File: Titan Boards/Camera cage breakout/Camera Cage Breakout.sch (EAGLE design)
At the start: 10 parts, among them IC1 LM741D, T2 2N2222

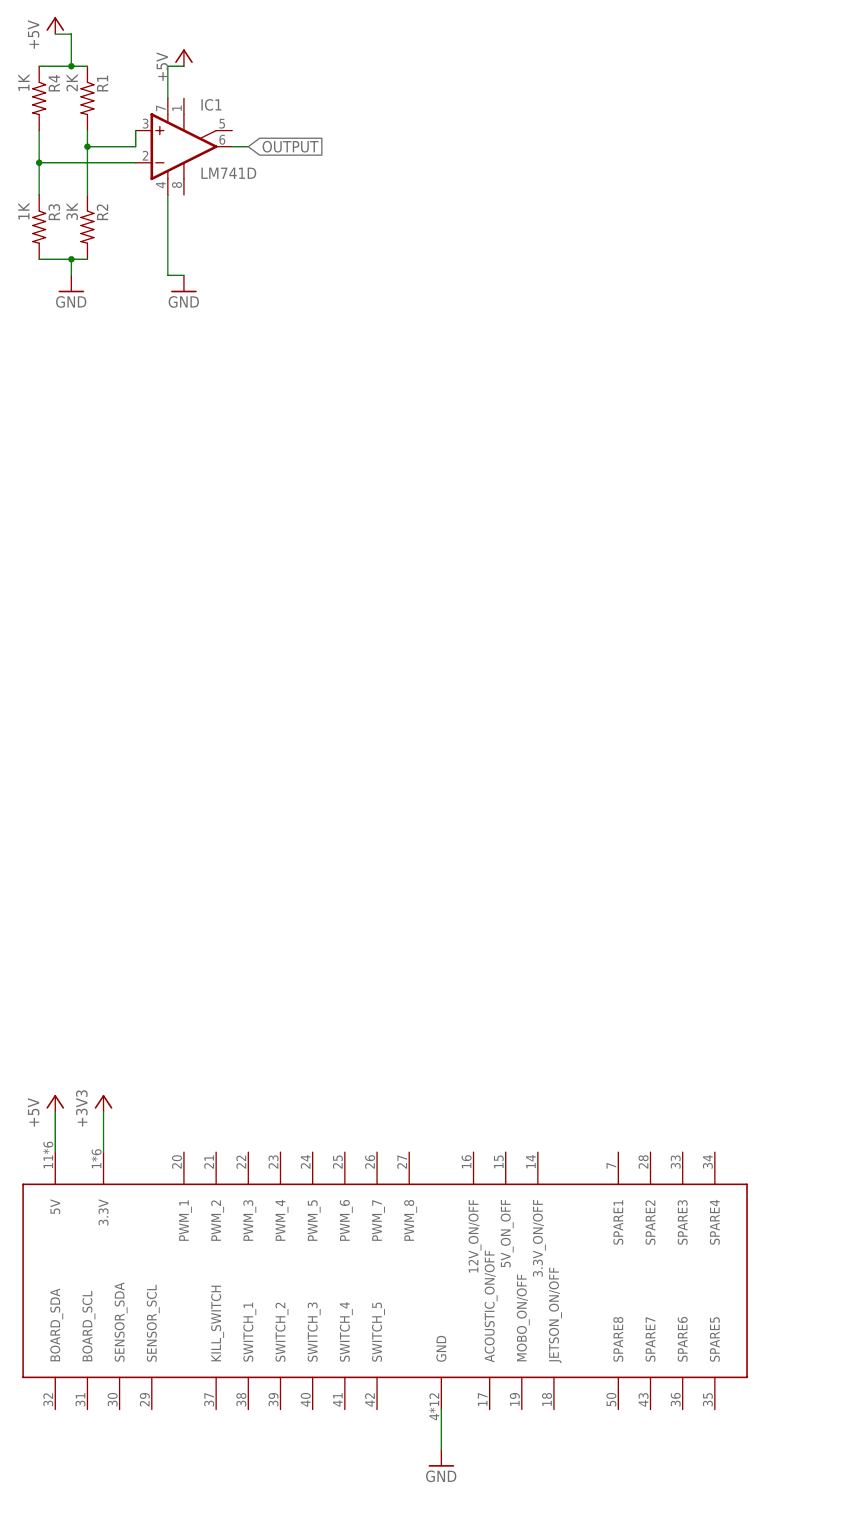
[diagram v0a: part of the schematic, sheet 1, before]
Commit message: Library added for 8 pin molex
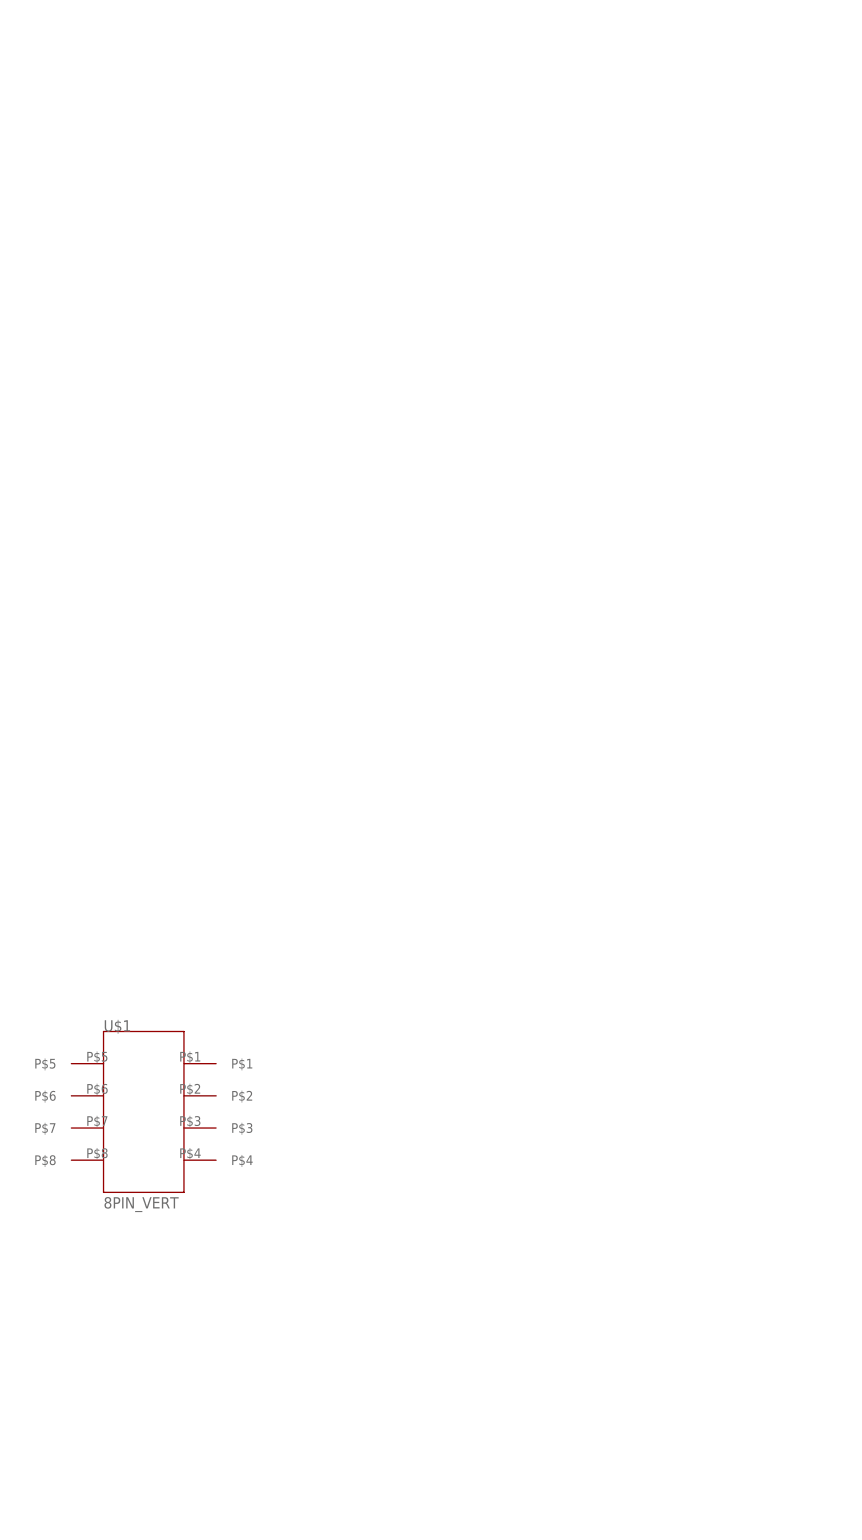
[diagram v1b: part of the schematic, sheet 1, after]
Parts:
- removed D2: green, SparkFun-LED:LED0603
- removed IC1: LM741D, linear:LM741D
- removed R1: 2K, rcl:R-US_R0603
- removed R2, R8: 3K, rcl:R-US_R0603
- removed R3, R4: 1K, rcl:R-US_R0603
- removed R7: 560, rcl:R-US_R0603
- removed T2: 2N2222, transistor:2N2222
- U$1: value 5530843-EDGE -> 8PIN_VERT; device 5530843-6:5530843-EDGE -> Vertical_Connectors:8PIN_VERT
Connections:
- removed net +3V3: U$1.3.3V
- removed net +5V: IC1.V+, R1.1, R4.1, T2.C, U$1.5V
- removed net GND: D2.C, IC1.V-, R2.2, R3.2, U$1.GND
- removed net N$1: IC1.-IN, R3.1, R4.2
- removed net N$2: IC1.+IN, R1.2, R2.1
- removed net N$3: R8.1, T2.B
- removed net N$7: R7.2, T2.E
- removed net N$8: D2.A, R7.1
- removed net OUTPUT: IC1.OUT, R8.2

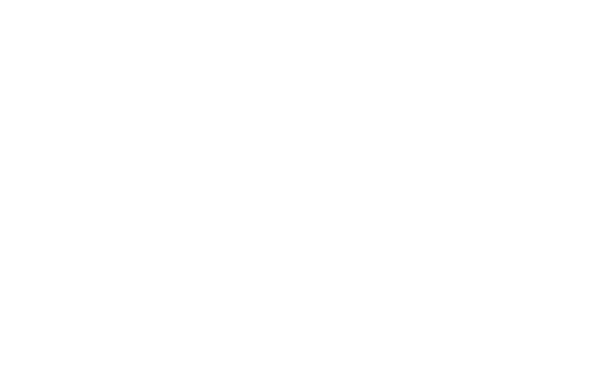
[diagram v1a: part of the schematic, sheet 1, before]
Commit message: updated library for cage breakout
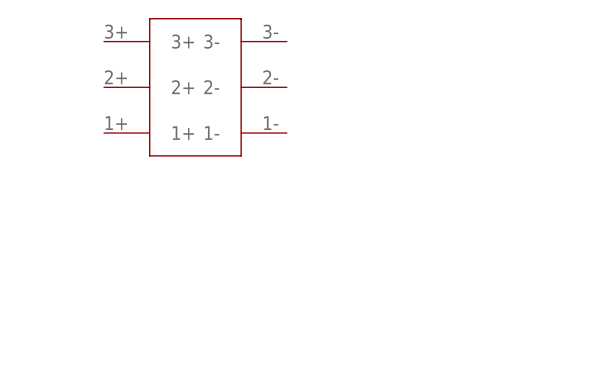
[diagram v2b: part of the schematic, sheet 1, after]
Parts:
- added U$2: 6PIN-VERT, Vertical_Connectors:6PIN-VERT
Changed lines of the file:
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@@
 <part name="FRAME2" library="frames" library_urn="urn:adsk.eagle:library:229" deviceset="A3L-LOC" device="" value="a"/>
 <part name="U$1" library="Vertical_Connectors" deviceset="8PIN_VERT" device=""/>
+<part name="U$2" library="Vertical_Connectors" deviceset="6PIN-VERT" device=""/>
 </parts>
 <sheets>
@@
 <attribute name="VALUE" x="38.1" y="55.88" size="1.778" layer="96"/>
 </instance>
+<instance part="U$2" gate="G$1" x="40.64" y="132.08" smashed="yes"/>
 </instances>
 <busses>

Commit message: schematic work for camera cage breakout
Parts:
- added MYNT_CAMERA_NETWORK_SWITCH, PELTIER_AND_FANS: 4PIN-VERT, Vertical_Connectors:4PIN-VERT
- added XAVIER: 2PIN-VERT, Vertical_Connectors:2PIN-VERT
- renumbered U$1 to EXTRA_POWER, U$2 to INPUT_POWER
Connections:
- new net 5V: MYNT_CAMERA_NETWORK_SWITCH.P$1, MYNT_CAMERA_NETWORK_SWITCH.P$2
- new net GND: MYNT_CAMERA_NETWORK_SWITCH.P$3, MYNT_CAMERA_NETWORK_SWITCH.P$4, PELTIER_AND_FANS.P$3, PELTIER_AND_FANS.P$4, XAVIER.P$2
- new net PELTIER_SWITCHED: PELTIER_AND_FANS.P$1, PELTIER_AND_FANS.P$2
- new net XAVIER_SWITCHED: XAVIER.P$1
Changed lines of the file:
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@@
 <part name="FRAME1" library="frames" library_urn="urn:adsk.eagle:library:229" deviceset="A3L-LOC" device="" value="a"/>
 <part name="FRAME2" library="frames" library_urn="urn:adsk.eagle:library:229" deviceset="A3L-LOC" device="" value="a"/>
-<part name="U$1" library="Vertical_Connectors" deviceset="8PIN_VERT" device=""/>
-<part name="U$2" library="Vertical_Connectors" deviceset="6PIN-VERT" device=""/>
+<part name="EXTRA_POWER" library="Vertical_Connectors" deviceset="8PIN_VERT" device=""/>
+<part name="INPUT_POWER" library="Vertical_Connectors" deviceset="6PIN-VERT" device=""/>
+<part name="XAVIER" library="Vertical_Connectors" deviceset="2PIN-VERT" device=""/>
+<part name="MYNT_CAMERA_NETWORK_SWITCH" library="Vertical_Connectors" deviceset="4PIN-VERT" device=""/>
+<part name="PELTIER_AND_FANS" library="Vertical_Connectors" deviceset="4PIN-VERT" device=""/>
 </parts>
 <sheets>
@@
 <attribute name="SHEET" x="357.680259375" y="4.9784" size="2.54" layer="94"/>
 </instance>
-<instance part="U$1" gate="G$1" x="38.1" y="83.82" smashed="yes">
+<instance part="EXTRA_POWER" gate="G$1" x="38.1" y="83.82" smashed="yes">
 <attribute name="NAME" x="38.1" y="83.82" size="1.778" layer="95"/>
 <attribute name="VALUE" x="38.1" y="55.88" size="1.778" layer="96"/>
 </instance>
-<instance part="U$2" gate="G$1" x="40.64" y="132.08" smashed="yes"/>
+<instance part="INPUT_POWER" gate="G$1" x="40.64" y="132.08" smashed="yes"/>
+<instance part="XAVIER" gate="G$1" x="121.92" y="58.42" smashed="yes">
+<attribute name="NAME" x="116.84" y="60.96" size="1.778" layer="95"/>
+</instance>
+<instance part="MYNT_CAMERA_NETWORK_SWITCH" gate="G$1" x="177.8" y="101.6" smashed="yes">
+<attribute name="NAME" x="175.26" y="111.76" size="1.778" layer="95"/>
+</instance>
+<instance part="PELTIER_AND_FANS" gate="G$1" x="177.8" y="81.28" smashed="yes">
+<attribute name="NAME" x="175.26" y="91.44" size="1.778" layer="95"/>
+</instance>
 </instances>
 <busses>
 </busses>
 <nets>
+<net name="GND" class="0">
+<segment>
+<pinref part="MYNT_CAMERA_NETWORK_SWITCH" gate="G$1" pin="P$3"/>
+<pinref part="MYNT_CAMERA_NETWORK_SWITCH" gate="G$1" pin="P$4"/>
+<wire x1="195.58" y1="109.22" x2="195.58" y2="106.68" width="0.1524" layer="91"/>
+<wire x1="195.58" y1="106.68" x2="195.58" y2="101.6" width="0.1524" layer="91"/>
+<wire x1="195.58" y1="106.68" x2="198.12" y2="106.68" width="0.1524" layer="91"/>
+<junction x="195.58" y="106.68"/>
+<label x="198.12" y="106.68" size="1.778" layer="95" xref="yes"/>
+</segment>
+<segment>
+<pinref part="PELTIER_AND_FANS" gate="G$1" pin="P$3"/>
+<pinref part="PELTIER_AND_FANS" gate="G$1" pin="P$4"/>
+<wire x1="195.58" y1="88.9" x2="195.58" y2="86.36" width="0.1524" layer="91"/>
+<wire x1="195.58" y1="86.36" x2="195.58" y2="81.28" width="0.1524" layer="91"/>
+<wire x1="195.58" y1="86.36" x2="198.12" y2="86.36" width="0.1524" layer="91"/>
+<junction x="195.58" y="86.36"/>
+<label x="198.12" y="86.36" size="1.778" layer="95" xref="yes"/>
+</segment>
+<segment>
+<pinref part="XAVIER" gate="G$1" pin="P$2"/>
+<wire x1="111.76" y1="53.34" x2="109.22" y2="53.34" width="0.1524" layer="91"/>
+<label x="109.22" y="53.34" size="1.778" layer="95" rot="R180" xref="yes"/>
+</segment>
+</net>
+<net name="5V" class="0">
+<segment>
+<pinref part="MYNT_CAMERA_NETWORK_SWITCH" gate="G$1" pin="P$1"/>
+<pinref part="MYNT_CAMERA_NETWORK_SWITCH" gate="G$1" pin="P$2"/>
+<wire x1="170.18" y1="109.22" x2="170.18" y2="106.68" width="0.1524" layer="91"/>
+<wire x1="170.18" y1="106.68" x2="170.18" y2="101.6" width="0.1524" layer="91"/>
+<wire x1="170.18" y1="106.68" x2="167.64" y2="106.68" width="0.1524" layer="91"/>
+<junction x="170.18" y="106.68"/>
+<label x="167.64" y="106.68" size="1.778" layer="95" rot="R180" xref="yes"/>
+</segment>
+</net>
+<net name="PELTIER_SWITCHED" class="0">
+<segment>
+<pinref part="PELTIER_AND_FANS" gate="G$1" pin="P$1"/>
+<pinref part="PELTIER_AND_FANS" gate="G$1" pin="P$2"/>
+<wire x1="170.18" y1="88.9" x2="170.18" y2="86.36" width="0.1524" layer="91"/>
+<wire x1="170.18" y1="86.36" x2="170.18" y2="81.28" width="0.1524" layer="91"/>
+<wire x1="170.18" y1="86.36" x2="167.64" y2="86.36" width="0.1524" layer="91"/>
+<junction x="170.18" y="86.36"/>
+<label x="167.64" y="86.36" size="1.778" layer="95" rot="R180" xref="yes"/>
+</segment>
+</net>
+<net name="XAVIER_SWITCHED" class="0">
+<segment>
+<pinref part="XAVIER" gate="G$1" pin="P$1"/>
+<wire x1="111.76" y1="58.42" x2="109.22" y2="58.42" width="0.1524" layer="91"/>
+<label x="109.22" y="58.42" size="1.778" layer="95" rot="R180" xref="yes"/>
+</segment>
+</net>
 </nets>
 </sheet>

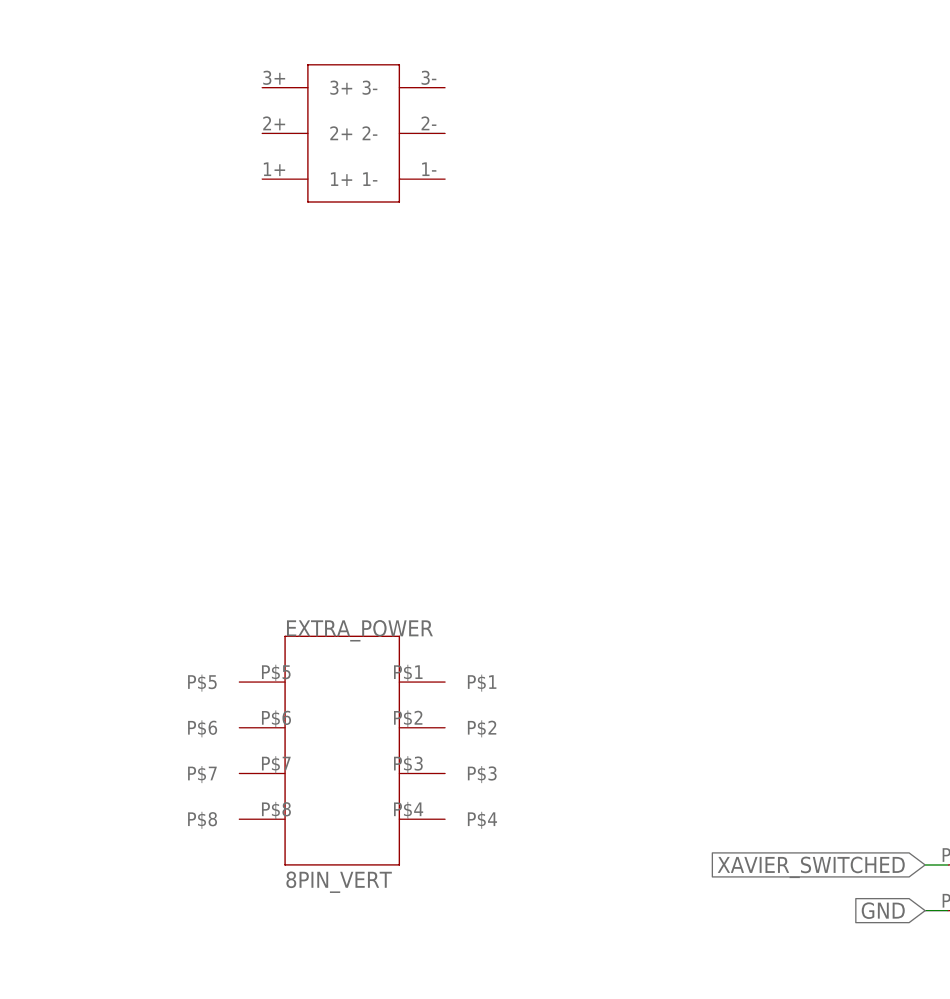
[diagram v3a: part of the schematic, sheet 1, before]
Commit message: schematic work for camera cage breakout
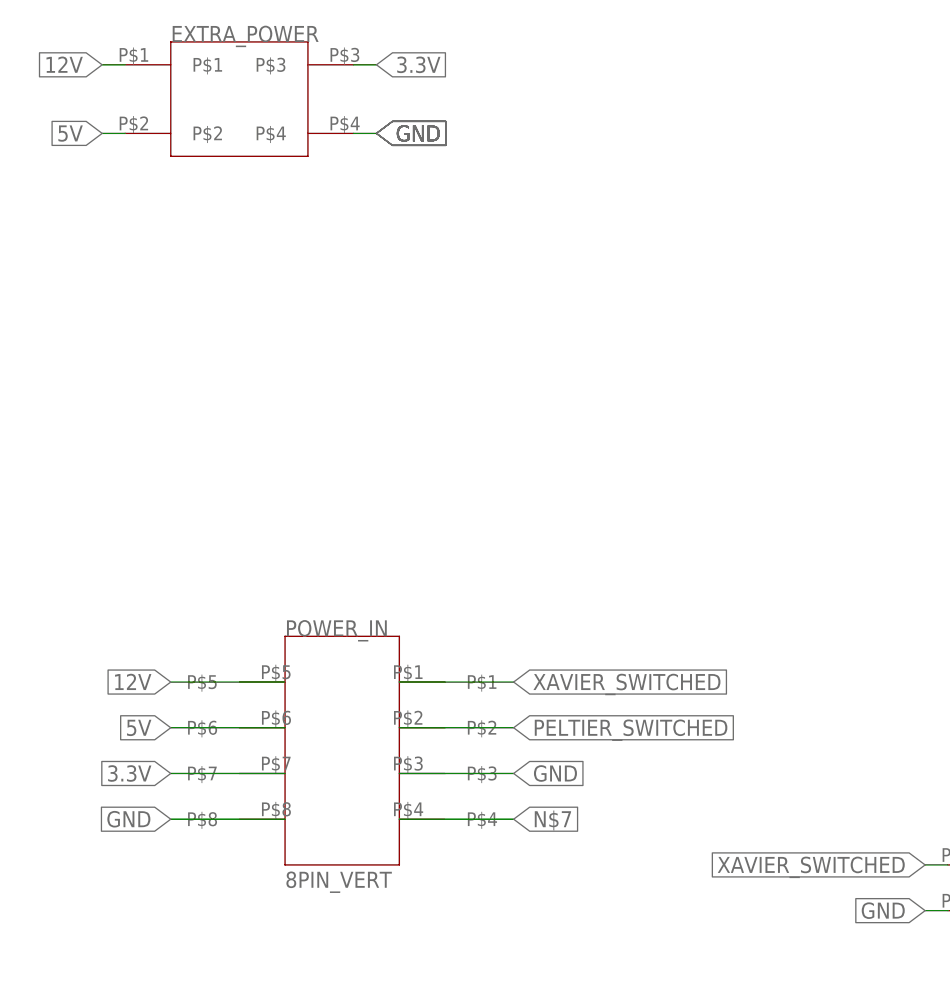
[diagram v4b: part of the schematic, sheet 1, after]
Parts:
- removed INPUT_POWER: 6PIN-VERT, Vertical_Connectors:6PIN-VERT
- added POWER_IN: 8PIN_VERT, Vertical_Connectors:8PIN_VERT
- EXTRA_POWER: value 8PIN_VERT -> 4PIN-VERT; device Vertical_Connectors:8PIN_VERT -> Vertical_Connectors:4PIN-VERT
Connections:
- new net 12V: EXTRA_POWER.P$1, POWER_IN.P$5
- new net 3.3V: EXTRA_POWER.P$3, POWER_IN.P$7
- new net N$7: POWER_IN.P$4
- net 5V: now also EXTRA_POWER.P$2, POWER_IN.P$6
- net GND: now also EXTRA_POWER.P$4, POWER_IN.P$3, POWER_IN.P$8
- net PELTIER_SWITCHED: now also POWER_IN.P$2
- net XAVIER_SWITCHED: now also POWER_IN.P$1
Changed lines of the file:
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@@
 <part name="FRAME1" library="frames" library_urn="urn:adsk.eagle:library:229" deviceset="A3L-LOC" device="" value="a"/>
 <part name="FRAME2" library="frames" library_urn="urn:adsk.eagle:library:229" deviceset="A3L-LOC" device="" value="a"/>
-<part name="EXTRA_POWER" library="Vertical_Connectors" deviceset="8PIN_VERT" device=""/>
-<part name="INPUT_POWER" library="Vertical_Connectors" deviceset="6PIN-VERT" device=""/>
+<part name="POWER_IN" library="Vertical_Connectors" deviceset="8PIN_VERT" device=""/>
 <part name="XAVIER" library="Vertical_Connectors" deviceset="2PIN-VERT" device=""/>
 <part name="MYNT_CAMERA_NETWORK_SWITCH" library="Vertical_Connectors" deviceset="4PIN-VERT" device=""/>
 <part name="PELTIER_AND_FANS" library="Vertical_Connectors" deviceset="4PIN-VERT" device=""/>
+<part name="EXTRA_POWER" library="Vertical_Connectors" deviceset="4PIN-VERT" device=""/>
 </parts>
 <sheets>
@@
 <attribute name="SHEET" x="357.680259375" y="4.9784" size="2.54" layer="94"/>
 </instance>
-<instance part="EXTRA_POWER" gate="G$1" x="38.1" y="83.82" smashed="yes">
+<instance part="POWER_IN" gate="G$1" x="38.1" y="83.82" smashed="yes">
 <attribute name="NAME" x="38.1" y="83.82" size="1.778" layer="95"/>
 <attribute name="VALUE" x="38.1" y="55.88" size="1.778" layer="96"/>
 </instance>
-<instance part="INPUT_POWER" gate="G$1" x="40.64" y="132.08" smashed="yes"/>
 <instance part="XAVIER" gate="G$1" x="121.92" y="58.42" smashed="yes">
 <attribute name="NAME" x="116.84" y="60.96" size="1.778" layer="95"/>
@@
 <instance part="PELTIER_AND_FANS" gate="G$1" x="177.8" y="81.28" smashed="yes">
 <attribute name="NAME" x="175.26" y="91.44" size="1.778" layer="95"/>
+</instance>
+<instance part="EXTRA_POWER" gate="G$1" x="27.94" y="139.7" smashed="yes">
+<attribute name="NAME" x="25.4" y="149.86" size="1.778" layer="95"/>
 </instance>
 </instances>
@@
 <label x="109.22" y="53.34" size="1.778" layer="95" rot="R180" xref="yes"/>
 </segment>
+<segment>
+<pinref part="POWER_IN" gate="G$1" pin="P$8"/>
+<wire x1="38.1" y1="63.5" x2="25.4" y2="63.5" width="0.1524" layer="91"/>
+<label x="25.4" y="63.5" size="1.778" layer="95" rot="R180" xref="yes"/>
+</segment>
+<segment>
+<pinref part="EXTRA_POWER" gate="G$1" pin="P$4"/>
+<wire x1="45.72" y1="139.7" x2="48.26" y2="139.7" width="0.1524" layer="91"/>
+<label x="48.26" y="139.7" size="1.778" layer="95" xref="yes"/>
+<label x="48.26" y="139.7" size="1.778" layer="95" xref="yes"/>
+<label x="48.26" y="139.7" size="1.778" layer="95" xref="yes"/>
+<label x="48.26" y="139.7" size="1.778" layer="95" xref="yes"/>
+</segment>
+<segment>
+<pinref part="POWER_IN" gate="G$1" pin="P$3"/>
+<wire x1="50.8" y1="68.58" x2="63.5" y2="68.58" width="0.1524" layer="91"/>
+<label x="63.5" y="68.58" size="1.778" layer="95" xref="yes"/>
+</segment>
 </net>
 <net name="5V" class="0">
@@
 <junction x="170.18" y="106.68"/>
 <label x="167.64" y="106.68" size="1.778" layer="95" rot="R180" xref="yes"/>
+</segment>
+<segment>
+<pinref part="POWER_IN" gate="G$1" pin="P$6"/>
+<wire x1="38.1" y1="73.66" x2="25.4" y2="73.66" width="0.1524" layer="91"/>
+<label x="25.4" y="73.66" size="1.778" layer="95" rot="R180" xref="yes"/>
+</segment>
+<segment>
+<pinref part="EXTRA_POWER" gate="G$1" pin="P$2"/>
+<wire x1="20.32" y1="139.7" x2="17.78" y2="139.7" width="0.1524" layer="91"/>
+<label x="17.78" y="139.7" size="1.778" layer="95" rot="R180" xref="yes"/>
 </segment>
 </net>
@@
 <label x="167.64" y="86.36" size="1.778" layer="95" rot="R180" xref="yes"/>
 </segment>
+<segment>
+<pinref part="POWER_IN" gate="G$1" pin="P$2"/>
+<wire x1="50.8" y1="73.66" x2="63.5" y2="73.66" width="0.1524" layer="91"/>
+<label x="63.5" y="73.66" size="1.778" layer="95" xref="yes"/>
+</segment>
 </net>
 <net name="XAVIER_SWITCHED" class="0">
@@
 <label x="109.22" y="58.42" size="1.778" layer="95" rot="R180" xref="yes"/>
 </segment>
+<segment>
+<pinref part="POWER_IN" gate="G$1" pin="P$1"/>
+<wire x1="50.8" y1="78.74" x2="63.5" y2="78.74" width="0.1524" layer="91"/>
+<label x="63.5" y="78.74" size="1.778" layer="95" xref="yes"/>
+</segment>
 </net>
+<net name="12V" class="0">
+<segment>
+<pinref part="POWER_IN" gate="G$1" pin="P$5"/>
+<wire x1="38.1" y1="78.74" x2="25.4" y2="78.74" width="0.1524" layer="91"/>
+<label x="25.4" y="78.74" size="1.778" layer="95" rot="R180" xref="yes"/>
+</segment>
+<segment>
+<pinref part="EXTRA_POWER" gate="G$1" pin="P$1"/>
+<wire x1="20.32" y1="147.32" x2="17.78" y2="147.32" width="0.1524" layer="91"/>
+<label x="17.78" y="147.32" size="1.778" layer="95" rot="R180" xref="yes"/>
+</segment>
+</net>
+<net name="3.3V" class="0">
+<segment>
+<pinref part="POWER_IN" gate="G$1" pin="P$7"/>
+<wire x1="38.1" y1="68.58" x2="25.4" y2="68.58" width="0.1524" layer="91"/>
+<label x="25.4" y="68.58" size="1.778" layer="95" rot="R180" xref="yes"/>
+</segment>
+<segment>
+<pinref part="EXTRA_POWER" gate="G$1" pin="P$3"/>
+<wire x1="45.72" y1="147.32" x2="48.26" y2="147.32" width="0.1524" layer="91"/>
+<label x="48.26" y="147.32" size="1.778" layer="95" xref="yes"/>
+</segment>
+</net>
+<net name="N$7" class="0">
+<segment>
+<pinref part="POWER_IN" gate="G$1" pin="P$4"/>
+<wire x1="50.8" y1="63.5" x2="63.5" y2="63.5" width="0.1524" layer="91"/>
+<label x="63.5" y="63.5" size="1.778" layer="95" xref="yes"/>
+</segment>
+</net>
